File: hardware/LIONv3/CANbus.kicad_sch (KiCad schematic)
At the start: 8 parts, among them U1 TCAN3414DR

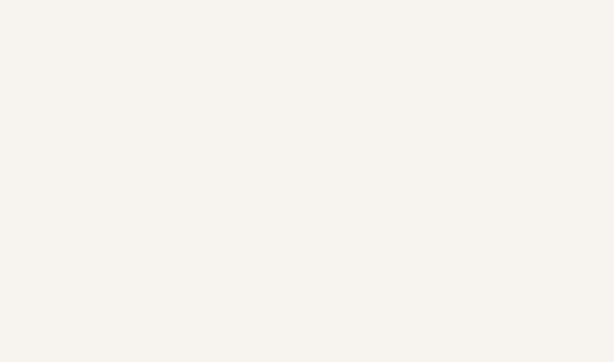
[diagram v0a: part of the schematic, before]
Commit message: refactor(hardware): reorganize schematic
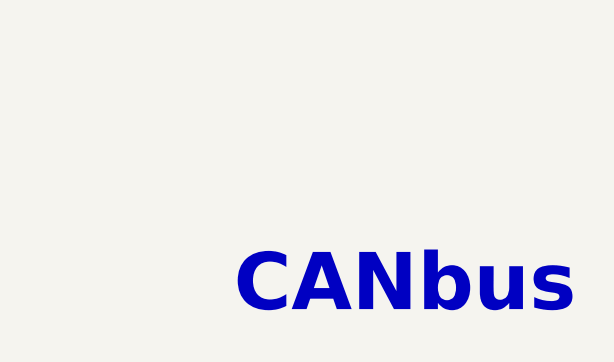
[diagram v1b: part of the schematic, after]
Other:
- note added: "CANbus"
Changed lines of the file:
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@@
+		)
+	)
+	(text "CANbus"
+		(exclude_from_sim no)
+		(at 242.57 151.13 0)
+		(effects
+			(font
+				(size 6.35 6.35)
+				(thickness 1.27)
+				(bold yes)
+			)
 		)
 	)

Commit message: feat(hardware): add pre-review schematic
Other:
- note added: "DEFAULT: OPEN TERMINATION"
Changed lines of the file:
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@@
+		)
+	)
+	(text "DEFAULT: OPEN TERMINATION"
+		(exclude_from_sim no)
+		(at 151.13 22.86 0)
+		(effects
+			(font
+				(size 1.27 1.27)
+			)
 		)
 	)

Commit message: feat(hardware): add TestPoints
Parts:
- renumbered C1 to C20, C2 to C21, C24 to C22, D1 to D6, R1 to R28, R12 to R29, U1 to U21
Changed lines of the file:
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@@
 		(title "LIONv3")
 		(date "2026-08-12")
-		(rev "0.1")
+		(rev "1.0")
 		(comment 1 "v3-Rodrigo")
 		(comment 2 "Rodrigo Andrade")
 		(comment 3 "2026-08-12")
+		(comment 4 "Rodrigo Andrade")
+		(comment 5 "2026-09-14")
 	)
 	(text "CAN_STB:\ndown -> ACTIVE\nup -> STANDBY"
@@
 	(wire
 		(pts
+			(xy 21.59 30.48) (xy 21.59 31.75)
+		)
+		(stroke
+			(width 0)
+			(type default)
+		)
+	)
+	(wire
+		(pts
+			(xy 156.21 31.75) (xy 161.29 31.75)
+		)
+		(stroke
+			(width 0)
+			(type default)
+		)
+	)
+	(wire
+		(pts
+			(xy 97.79 31.75) (xy 102.87 31.75)
+		)
+		(stroke
+			(width 0)
+			(type default)
+		)
+	)
+	(wire
+		(pts
 			(xy 80.01 31.75) (xy 97.79 31.75)
-		)
-		(stroke
-			(width 0)
-			(type default)
-		)
-	)
-	(wire
-		(pts
-			(xy 21.59 30.48) (xy 21.59 31.75)
-		)
-		(stroke
-			(width 0)
-			(type default)
-		)
-	)
-	(wire
-		(pts
-			(xy 156.21 31.75) (xy 161.29 31.75)
-		)
-		(stroke
-			(width 0)
-			(type default)
-		)
-	)
-	(wire
-		(pts
-			(xy 97.79 31.75) (xy 102.87 31.75)
 		)
 		(stroke
@@
 		(dnp no)
 		(fields_autoplaced yes)
-		(property "Reference" "C1"
+		(property "Reference" "C20"
 			(at 24.13 36.8362 0)
 			(show_name no)
@@
 			(project "LIONv3"
 				(path "/3cc9e06f-00d0-4bec-822f-2e156022ced4/732ad377-cd6b-418c-b5b5-46888f6f133e"
-					(reference "C1")
+					(reference "C20")
 					(unit 1)
 				)
@@
 		(dnp no)
 		(fields_autoplaced yes)
-		(property "Reference" "R1"
+		(property "Reference" "R28"
 			(at 139.7 26.67 90)
 			(show_name no)
@@
 			(project "LIONv3"
 				(path "/3cc9e06f-00d0-4bec-822f-2e156022ced4/732ad377-cd6b-418c-b5b5-46888f6f133e"
-					(reference "R1")
+					(reference "R28")
 					(unit 1)
 				)
@@
 		(dnp no)
 		(fields_autoplaced yes)
-		(property "Reference" "R12"
+		(property "Reference" "R29"
 			(at 163.83 26.67 90)
 			(show_name no)
@@
 			(project "LIONv3"
 				(path "/3cc9e06f-00d0-4bec-822f-2e156022ced4/732ad377-cd6b-418c-b5b5-46888f6f133e"
-					(reference "R12")
+					(reference "R29")
 					(unit 1)
 				)
@@
 		(dnp no)
 		(fields_autoplaced yes)
-		(property "Reference" "D1"
+		(property "Reference" "D6"
 			(at 97.79 41.9099 0)
 			(show_name no)
@@
 			)
 		)
-		(property "Datasheet" "https://www.st.com/resource/en/datasheet/esdal.pdf"
+		(property "Datasheet" "file://${KIPRJMOD}/LIONv3-Datasheets/TI-ESD752DBZR.pdf"
 			(at 91.44 58.42 0)
 			(hide yes)
@@
 			(project "LIONv3"
 				(path "/3cc9e06f-00d0-4bec-822f-2e156022ced4/732ad377-cd6b-418c-b5b5-46888f6f133e"
-					(reference "D1")
+					(reference "D6")
 					(unit 1)
 				)
@@
 		(in_pos_files yes)
 		(dnp no)
-		(property "Reference" "#PWR05"
+		(property "Reference" "#PWR058"
 			(at 21.59 52.07 0)
 			(hide yes)
@@
 			(project "LIONv3"
 				(path "/3cc9e06f-00d0-4bec-822f-2e156022ced4/732ad377-cd6b-418c-b5b5-46888f6f133e"
-					(reference "#PWR05")
+					(reference "#PWR058")
 					(unit 1)
 				)
@@
 		(dnp no)
 		(fields_autoplaced yes)
-		(property "Reference" "#PWR01"
+		(property "Reference" "#PWR056"
 			(at 21.59 34.29 0)
 			(hide yes)
@@
 			(project "LIONv3"
 				(path "/3cc9e06f-00d0-4bec-822f-2e156022ced4/732ad377-cd6b-418c-b5b5-46888f6f133e"
-					(reference "#PWR01")
+					(reference "#PWR056")
 					(unit 1)
 				)
@@
 		(dnp no)
 		(fields_autoplaced yes)
-		(property "Reference" "#PWR020"
+		(property "Reference" "#PWR057"
 			(at 151.13 49.53 0)
 			(hide yes)
@@
 			(project "LIONv3"
 				(path "/3cc9e06f-00d0-4bec-822f-2e156022ced4/732ad377-cd6b-418c-b5b5-46888f6f133e"
-					(reference "#PWR020")
+					(reference "#PWR057")
 					(unit 1)
 				)
@@
 		(dnp no)
 		(fields_autoplaced yes)
-		(property "Reference" "C24"
+		(property "Reference" "C22"
 			(at 153.67 38.0935 0)
 			(show_name no)
@@
 			(project "LIONv3"
 				(path "/3cc9e06f-00d0-4bec-822f-2e156022ced4/732ad377-cd6b-418c-b5b5-46888f6f133e"
-					(reference "C24")
+					(reference "C22")
 					(unit 1)
 				)
@@
 		(dnp no)
 		(fields_autoplaced yes)
-		(property "Reference" "C2"
+		(property "Reference" "C21"
 			(at 35.56 36.8362 0)
 			(show_name no)
@@
 			(project "LIONv3"
 				(path "/3cc9e06f-00d0-4bec-822f-2e156022ced4/732ad377-cd6b-418c-b5b5-46888f6f133e"
-					(reference "C2")
+					(reference "C21")
 					(unit 1)
 				)
@@
 		(in_pos_files yes)
 		(dnp no)
-		(property "Reference" "U1"
+		(property "Reference" "U21"
 			(at 67.31 24.13 0)
 			(show_name no)
@@
 			)
 		)
-		(property "Datasheet" "https://www.ti.com/lit/ds/symlink/tcan3414.pdf"
+		(property "Datasheet" "file://${KIPRJMOD}/LIONv3-Datasheets/TCAN3414DR.pdf"
 			(at 65.024 36.703 0)
 			(hide yes)
@@
 			(project "LIONv3"
 				(path "/3cc9e06f-00d0-4bec-822f-2e156022ced4/732ad377-cd6b-418c-b5b5-46888f6f133e"
-					(reference "U1")
+					(reference "U21")
 					(unit 1)
 				)

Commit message: feat(hardware): start PCB design
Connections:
- net CAN_N: now also D6.2 (K); no longer D6.1 (K)
- net CAN_P: now also D6.1 (K); no longer D6.2 (K)
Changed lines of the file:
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@@
 	)
 	(junction
-		(at 93.98 31.75)
-		(diameter 0)
-		(color 0 0 0 0)
-	)
-	(junction
-		(at 88.9 34.29)
+		(at 93.98 34.29)
 		(diameter 0)
 		(color 0 0 0 0)
@@
 	)
 	(junction
+		(at 88.9 31.75)
+		(diameter 0)
+		(color 0 0 0 0)
+	)
+	(junction
 		(at 21.59 44.45)
 		(diameter 0)
@@
 	(wire
 		(pts
-			(xy 88.9 34.29) (xy 100.33 34.29)
+			(xy 80.01 34.29) (xy 93.98 34.29)
 		)
 		(stroke
@@
 	(wire
 		(pts
-			(xy 93.98 38.1) (xy 93.98 31.75)
-		)
-		(stroke
-			(width 0)
-			(type default)
-		)
-	)
-	(wire
-		(pts
 			(xy 21.59 31.75) (xy 33.02 31.75)
 		)
@@
 	(wire
 		(pts
-			(xy 80.01 34.29) (xy 88.9 34.29)
-		)
-		(stroke
-			(width 0)
-			(type default)
-		)
-	)
-	(wire
-		(pts
 			(xy 80.01 39.37) (xy 81.28 39.37)
 		)
@@
 	(wire
 		(pts
+			(xy 88.9 31.75) (xy 97.79 31.75)
+		)
+		(stroke
+			(width 0)
+			(type default)
+		)
+	)
+	(wire
+		(pts
+			(xy 93.98 34.29) (xy 93.98 38.1)
+		)
+		(stroke
+			(width 0)
+			(type default)
+		)
+	)
+	(wire
+		(pts
 			(xy 21.59 30.48) (xy 21.59 31.75)
 		)
@@
 	(wire
 		(pts
-			(xy 80.01 31.75) (xy 97.79 31.75)
+			(xy 80.01 31.75) (xy 88.9 31.75)
 		)
 		(stroke
@@
 	(wire
 		(pts
+			(xy 93.98 34.29) (xy 100.33 34.29)
+		)
+		(stroke
+			(width 0)
+			(type default)
+		)
+	)
+	(wire
+		(pts
 			(xy 52.07 39.37) (xy 52.07 44.45)
 		)
@@
 	(wire
 		(pts
-			(xy 88.9 34.29) (xy 88.9 38.1)
-		)
-		(stroke
-			(width 0)
-			(type default)
-		)
-	)
-	(wire
-		(pts
 			(xy 50.8 36.83) (xy 54.61 36.83)
 		)
@@
 		)
 		(stroke
+			(width 0)
+			(type default)
+		)
+	)
+	(wire
+		(pts
+			(xy 88.9 31.75) (xy 88.9 38.1)
+		)
+		(stroke

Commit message: feat(hardware): route USB-C and CANbus differential pairs
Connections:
- net CAN_N: now also D6.1 (K); no longer D6.2 (K)
- net CAN_P: now also D6.2 (K); no longer D6.1 (K)
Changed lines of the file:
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@@
 	)
 	(junction
-		(at 93.98 34.29)
+		(at 88.9 34.29)
+		(diameter 0)
+		(color 0 0 0 0)
+	)
+	(junction
+		(at 93.98 31.75)
 		(diameter 0)
 		(color 0 0 0 0)
@@
 	)
 	(junction
-		(at 88.9 31.75)
-		(diameter 0)
-		(color 0 0 0 0)
-	)
-	(junction
 		(at 21.59 44.45)
 		(diameter 0)
@@
 	(wire
 		(pts
+			(xy 88.9 34.29) (xy 88.9 38.1)
+		)
+		(stroke
+			(width 0)
+			(type default)
+		)
+	)
+	(wire
+		(pts
 			(xy 33.02 31.75) (xy 33.02 35.56)
 		)
@@
 	(wire
 		(pts
-			(xy 80.01 34.29) (xy 93.98 34.29)
+			(xy 80.01 34.29) (xy 88.9 34.29)
+		)
+		(stroke
+			(width 0)
+			(type default)
+		)
+	)
+	(wire
+		(pts
+			(xy 93.98 31.75) (xy 93.98 38.1)
+		)
+		(stroke
+			(width 0)
+			(type default)
+		)
+	)
+	(wire
+		(pts
+			(xy 88.9 34.29) (xy 100.33 34.29)
 		)
 		(stroke
@@
 	(wire
 		(pts
-			(xy 88.9 31.75) (xy 97.79 31.75)
-		)
-		(stroke
-			(width 0)
-			(type default)
-		)
-	)
-	(wire
-		(pts
-			(xy 93.98 34.29) (xy 93.98 38.1)
-		)
-		(stroke
-			(width 0)
-			(type default)
-		)
-	)
-	(wire
-		(pts
 			(xy 21.59 30.48) (xy 21.59 31.75)
 		)
@@
 	(wire
 		(pts
-			(xy 80.01 31.75) (xy 88.9 31.75)
+			(xy 80.01 31.75) (xy 93.98 31.75)
 		)
 		(stroke
@@
 	(wire
 		(pts
+			(xy 93.98 31.75) (xy 97.79 31.75)
+		)
+		(stroke
+			(width 0)
+			(type default)
+		)
+	)
+	(wire
+		(pts
 			(xy 151.13 36.83) (xy 151.13 35.56)
 		)
@@
 	(wire
 		(pts
-			(xy 93.98 34.29) (xy 100.33 34.29)
-		)
-		(stroke
-			(width 0)
-			(type default)
-		)
-	)
-	(wire
-		(pts
 			(xy 52.07 39.37) (xy 52.07 44.45)
 		)
@@
 		)
 		(stroke
-			(width 0)
-			(type default)
-		)
-	)
-	(wire
-		(pts
-			(xy 88.9 31.75) (xy 88.9 38.1)
-		)
-		(stroke
